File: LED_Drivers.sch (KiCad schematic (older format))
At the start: 68 parts

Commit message: Started assigning footprints. Much cheaper to use the two channel n-fet for led driving. Need to change schematic to reflec.
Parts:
- J4: renamed from J?; footprint (none) -> Connectors_Phoenix:PhoenixContact_MC-GF_09x3.50mm_Angled_ThreadedFlange
- J5, J6, J7: renamed from J?; footprint (none) -> Connectors_Phoenix:PhoenixContact_MC-GF_08x3.50mm_Angled_ThreadedFlange
- Q1, Q10, Q11, Q12, Q13, Q14, Q15, Q16, Q17, Q18, Q19, Q2, Q20, Q21, Q22, Q23, Q24, Q25, Q26, Q27, Q28, Q29, Q3, Q30, Q31, Q32, Q4, Q5, Q6, Q7, Q8, Q9: renamed from Q?; footprint (none) -> TO_SOT_Packages_SMD:SOT-23_Handsoldering
- R11, R12, R13, R14, R15, R16, R17, R18, R19, R20, R21, R22, R23, R24, R25, R26, R27, R28, R29, R30, R31, R32, R33, R34, R35, R36, R37, R38, R39, R40, R41, R42: renamed from R?; footprint (none) -> Resistors_SMD:R_0603_HandSoldering

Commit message: Finished component footprint assignments and began rough layout of components.
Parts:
- removed Q1, Q10, Q11, Q12, Q13, Q14, Q15, Q16, Q17, Q18, Q19, Q2, Q20, Q21, Q22, Q23, Q24, Q25, Q26, Q27, Q28, Q29, Q3, Q30, Q31, Q32, Q4, Q5, Q6, Q7, Q8, Q9: Q_NMOS_GDS, TO_SOT_Packages_SMD:SOT-23_Handsoldering, symbol Q_NMOS_GDS
- added U10, U12, U13, U14, U15, U16, U17, U18, U19, U20, U21, U22, U23, U7, U8, U9: NUD3124, TO_SOT_Packages_SMD:SOT-23-6_Handsoldering, symbol NUD3124
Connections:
- wire segments 230 -> 229
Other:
- note removed: "USE SZNUD3124 FOR N-CHANNEL FET"

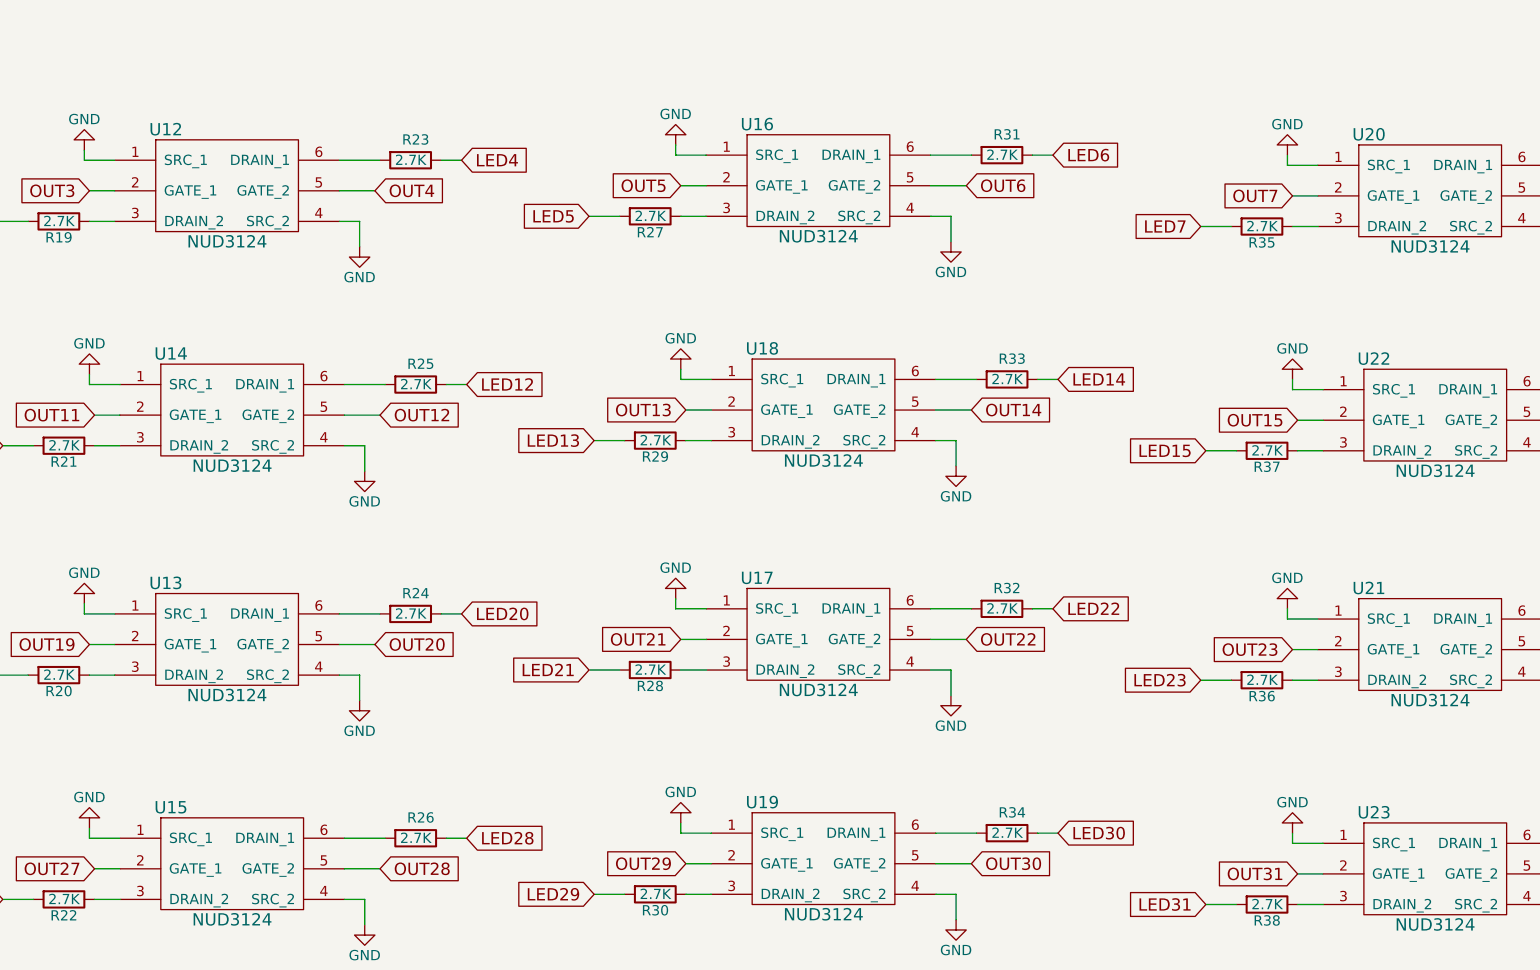
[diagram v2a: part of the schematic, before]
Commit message: Routed power, clock, switches and started on arduino/IO expanders
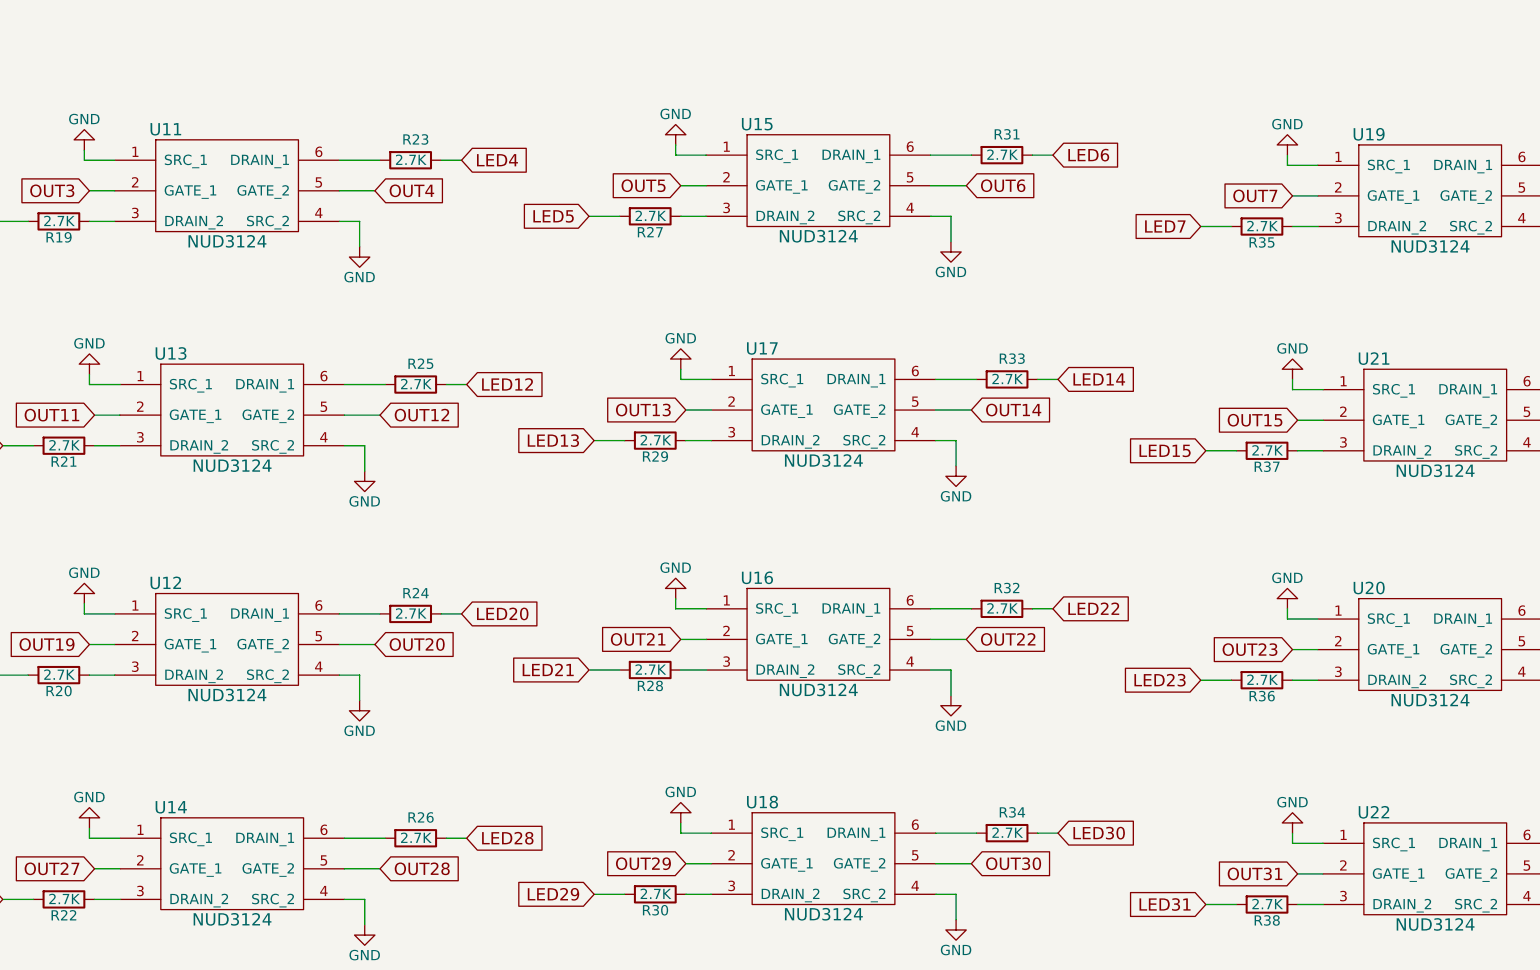
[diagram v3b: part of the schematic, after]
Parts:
- renumbered U12 to U11, U13 to U12, U14 to U13, U15 to U14, U16 to U15, U17 to U16, U18 to U17, U19 to U18, U20 to U19, U21 to U20, U22 to U21, U23 to U22
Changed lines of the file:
@@
 	7900 3050 8000 3050
 $Comp
-L NUD3124 U16
+L NUD3124 U15
 U 1 1 59F2EB75
 P 9800 3925
-F 0 "U16" H 9450 4975 60  0000 C CNN
+F 0 "U15" H 9450 4975 60  0000 C CNN
 F 1 "NUD3124" H 9750 4425 60  0000 C CNN
 F 2 "TO_SOT_Packages_SMD:SOT-23-6_Handsoldering" H 9800 3925 60  0001 C CNN
@@
 	10800 3025 10900 3025
 $Comp
-L NUD3124 U20
+L NUD3124 U19
 U 1 1 59F2EBA1
 P 12800 3975
-F 0 "U20" H 12450 5025 60  0000 C CNN
+F 0 "U19" H 12450 5025 60  0000 C CNN
 F 1 "NUD3124" H 12750 4475 60  0000 C CNN
 F 2 "TO_SOT_Packages_SMD:SOT-23-6_Handsoldering" H 12800 3975 60  0001 C CNN
@@
 	7925 4150 8025 4150
 $Comp
-L NUD3124 U18
+L NUD3124 U17
 U 1 1 59F2FD58
 P 9825 5025
-F 0 "U18" H 9475 6075 60  0000 C CNN
+F 0 "U17" H 9475 6075 60  0000 C CNN
 F 1 "NUD3124" H 9775 5525 60  0000 C CNN
 F 2 "TO_SOT_Packages_SMD:SOT-23-6_Handsoldering" H 9825 5025 60  0001 C CNN
@@
 	10825 4125 10925 4125
 $Comp
-L NUD3124 U22
+L NUD3124 U21
 U 1 1 59F2FD84
 P 12825 5075
-F 0 "U22" H 12475 6125 60  0000 C CNN
+F 0 "U21" H 12475 6125 60  0000 C CNN
 F 1 "NUD3124" H 12775 5575 60  0000 C CNN
 F 2 "TO_SOT_Packages_SMD:SOT-23-6_Handsoldering" H 12825 5075 60  0001 C CNN
@@
 	4900 5225 5000 5225
 $Comp
-L NUD3124 U13
+L NUD3124 U12
 U 1 1 59F2FFDB
 P 6900 6175
-F 0 "U13" H 6550 7225 60  0000 C CNN
+F 0 "U12" H 6550 7225 60  0000 C CNN
 F 1 "NUD3124" H 6850 6675 60  0000 C CNN
 F 2 "TO_SOT_Packages_SMD:SOT-23-6_Handsoldering" H 6900 6175 60  0001 C CNN
@@
 	7900 5275 8000 5275
 $Comp
-L NUD3124 U17
+L NUD3124 U16
 U 1 1 59F30007
 P 9800 6150
-F 0 "U17" H 9450 7200 60  0000 C CNN
+F 0 "U16" H 9450 7200 60  0000 C CNN
 F 1 "NUD3124" H 9750 6650 60  0000 C CNN
 F 2 "TO_SOT_Packages_SMD:SOT-23-6_Handsoldering" H 9800 6150 60  0001 C CNN
@@
 	10800 5250 10900 5250
 $Comp
-L NUD3124 U21
+L NUD3124 U20
 U 1 1 59F30033
 P 12800 6200
-F 0 "U21" H 12450 7250 60  0000 C CNN
+F 0 "U20" H 12450 7250 60  0000 C CNN
 F 1 "NUD3124" H 12750 6700 60  0000 C CNN
 F 2 "TO_SOT_Packages_SMD:SOT-23-6_Handsoldering" H 12800 6200 60  0001 C CNN
@@
 	4925 6325 5025 6325
 $Comp
-L NUD3124 U15
+L NUD3124 U14
 U 1 1 59F3008A
 P 6925 7275
-F 0 "U15" H 6575 8325 60  0000 C CNN
+F 0 "U14" H 6575 8325 60  0000 C CNN
 F 1 "NUD3124" H 6875 7775 60  0000 C CNN
 F 2 "TO_SOT_Packages_SMD:SOT-23-6_Handsoldering" H 6925 7275 60  0001 C CNN
@@
 	7925 6375 8025 6375
 $Comp
-L NUD3124 U19
+L NUD3124 U18
 U 1 1 59F300B6
 P 9825 7250
-F 0 "U19" H 9475 8300 60  0000 C CNN
+F 0 "U18" H 9475 8300 60  0000 C CNN
 F 1 "NUD3124" H 9775 7750 60  0000 C CNN
 F 2 "TO_SOT_Packages_SMD:SOT-23-6_Handsoldering" H 9825 7250 60  0001 C CNN
@@
 	10825 6350 10925 6350
 $Comp
-L NUD3124 U23
+L NUD3124 U22
 U 1 1 59F300E2
 P 12825 7300
-F 0 "U23" H 12475 8350 60  0000 C CNN
+F 0 "U22" H 12475 8350 60  0000 C CNN
 F 1 "NUD3124" H 12775 7800 60  0000 C CNN
 F 2 "TO_SOT_Packages_SMD:SOT-23-6_Handsoldering" H 12825 7300 60  0001 C CNN
@@
 $EndComp
 $Comp
-L NUD3124 U14
+L NUD3124 U13
 U 1 1 59F33702
 P 6925 5050
-F 0 "U14" H 6575 6100 60  0000 C CNN
+F 0 "U13" H 6575 6100 60  0000 C CNN
 F 1 "NUD3124" H 6875 5550 60  0000 C CNN
 F 2 "TO_SOT_Packages_SMD:SOT-23-6_Handsoldering" H 6925 5050 60  0001 C CNN
@@
 $EndComp
 $Comp
-L NUD3124 U12
+L NUD3124 U11
 U 1 1 59F337FE
 P 6900 3950
-F 0 "U12" H 6550 5000 60  0000 C CNN
+F 0 "U11" H 6550 5000 60  0000 C CNN
 F 1 "NUD3124" H 6850 4450 60  0000 C CNN
 F 2 "TO_SOT_Packages_SMD:SOT-23-6_Handsoldering" H 6900 3950 60  0001 C CNN

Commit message: Finished routing board.
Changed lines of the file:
@@
 L +12V #PWR049
 U 1 1 59E58249
-P 1350 2800
-F 0 "#PWR049" H 1350 2650 50  0001 C CNN
-F 1 "+12V" H 1350 2940 50  0000 C CNN
-F 2 "" H 1350 2800 50  0001 C CNN
-F 3 "" H 1350 2800 50  0001 C CNN
-	1    1350 2800
+P 1350 2750
+F 0 "#PWR049" H 1350 2600 50  0001 C CNN
+F 1 "+12V" H 1350 2890 50  0000 C CNN
+F 2 "" H 1350 2750 50  0001 C CNN
+F 3 "" H 1350 2750 50  0001 C CNN
+	1    1350 2750
 	1    0    0    -1
 $EndComp
 Wire Wire Line
-	1200 2850 1350 2850
+	1350 2850 1200 2850
 Wire Wire Line
-	1350 2850 1350 2800
+	1350 2750 1350 2850
 $Comp
 L GND #PWR050

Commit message: Started placing and routing new board with updated schematic. Requries RTC.
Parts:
- removed J4: Conn_01x09, Connectors_Phoenix:PhoenixContact_MC-GF_09x3.50mm_Angled_ThreadedFlange, symbol Conn_01x09
- removed J5, J6, J7: Conn_01x08, Connectors_Phoenix:PhoenixContact_MC-GF_08x3.50mm_Angled_ThreadedFlange, symbol Conn_01x08
- added J3, J4, J5, J6, J7, J8, J9: Conn_02x03_Odd_Even, Pin_Headers:Pin_Header_Straight_2x03_Pitch2.54mm, symbol Conn_02x03_Odd_Even
- renumbered R11 to R10, R12 to R11, R13 to R12, R14 to R13, R15 to R14, R16 to R15, R17 to R16, R18 to R17, R19 to R18, R20 to R19, R21 to R20, R22 to R21, R23 to R22, R24 to R23, R25 to R24, R26 to R25, R27 to R26, R28 to R27, R29 to R28, R30 to R29, R31 to R30, R32 to R31, R33 to R32, R34 to R33, R35 to R34, R36 to R35, R37 to R36, R38 to R37, R39 to R38, R40 to R39, R41 to R40, R42 to R41, U11 to U10, U12 to U11, U13 to U12, U14 to U13, U15 to U14, U16 to U15, U17 to U16, U18 to U17, U19 to U18, U20 to U19, U21 to U20, U22 to U21, U7 to U6, U8 to U7, U9 to U8, U10 to U9
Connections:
- net labels added: LED_PWR
- net labels removed: +12V, 12V
- wire segments 229 -> 199
- no-connect marks 0 -> 3
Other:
- note removed: "SHEET INPUTS\n"
- moved on the sheet: R10, R11, R12, R13, R14, R15, R16, R17, R18, R19, R20, R21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
